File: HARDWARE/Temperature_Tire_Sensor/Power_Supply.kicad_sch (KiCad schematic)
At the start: 8 parts

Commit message: A completed schematic
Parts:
- removed C?: 0.1uF, symbol Device:C
- removed C?: 47nF, symbol Device:C
- removed C?: 10uF, symbol Device:C
- removed IC?: NCV8775CDT33RKG, NCV8775CDT33RKG, symbol NCV8775CDT33RKG:NCV8775CDT33RKG
- removed R?: 5k, symbol Device:R_US
- added C?: 10u <3.4Ohm, symbol Device:C
- added FB?: 60R@100MHz, symbol Device:FerriteBead_Small
- added U?: MIC5236, symbol Regulator_Linear:LP38512TJ-1.8
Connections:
- net +24V: now also U?.1 (EN), U?.2 (IN)
- net +3V3: now also C?.1, FB?.1, U?.4 (OUT); no longer C?.1, U?.1 (VIN), U?.3 (EN)
- net GND: now also C?.2, U?.3 (GND), U?.6 (GND)
- new net: C?.1, FB?.2, U?.1 (VIN), U?.3 (EN)
- no-connect marks 0 -> 1

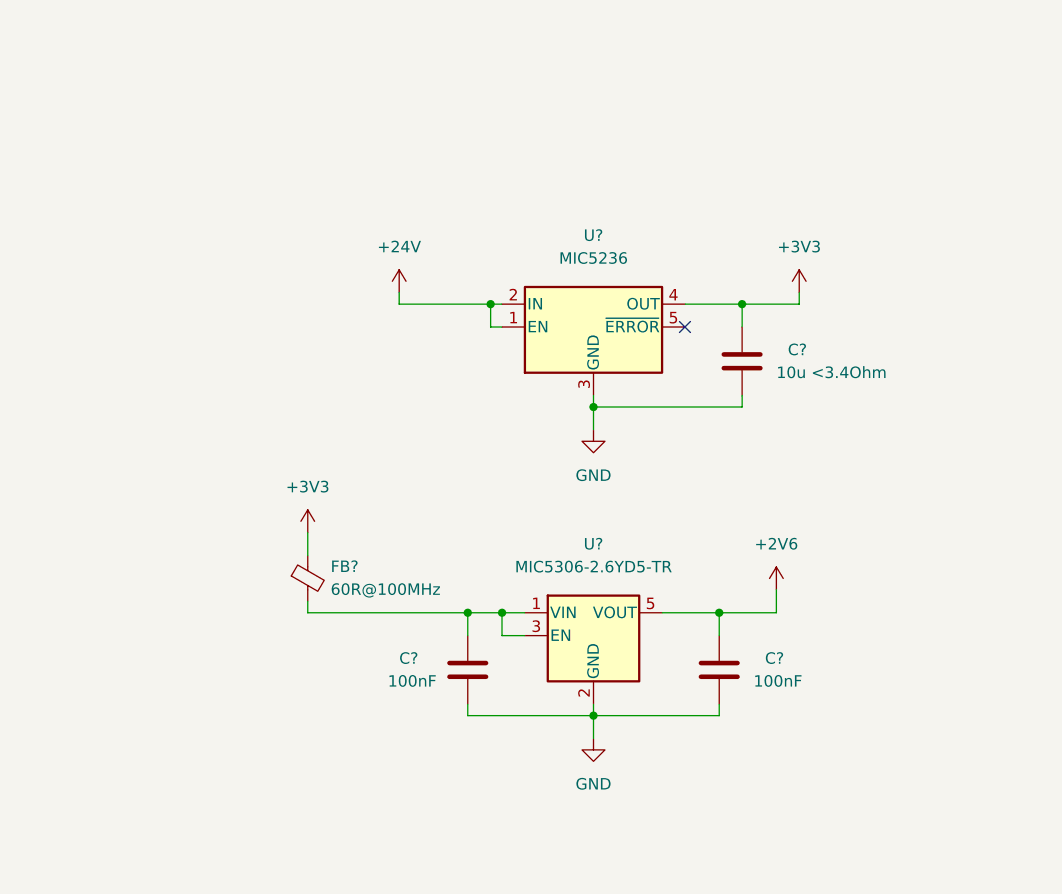
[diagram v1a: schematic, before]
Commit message: Changed the used type of labels and added power flags
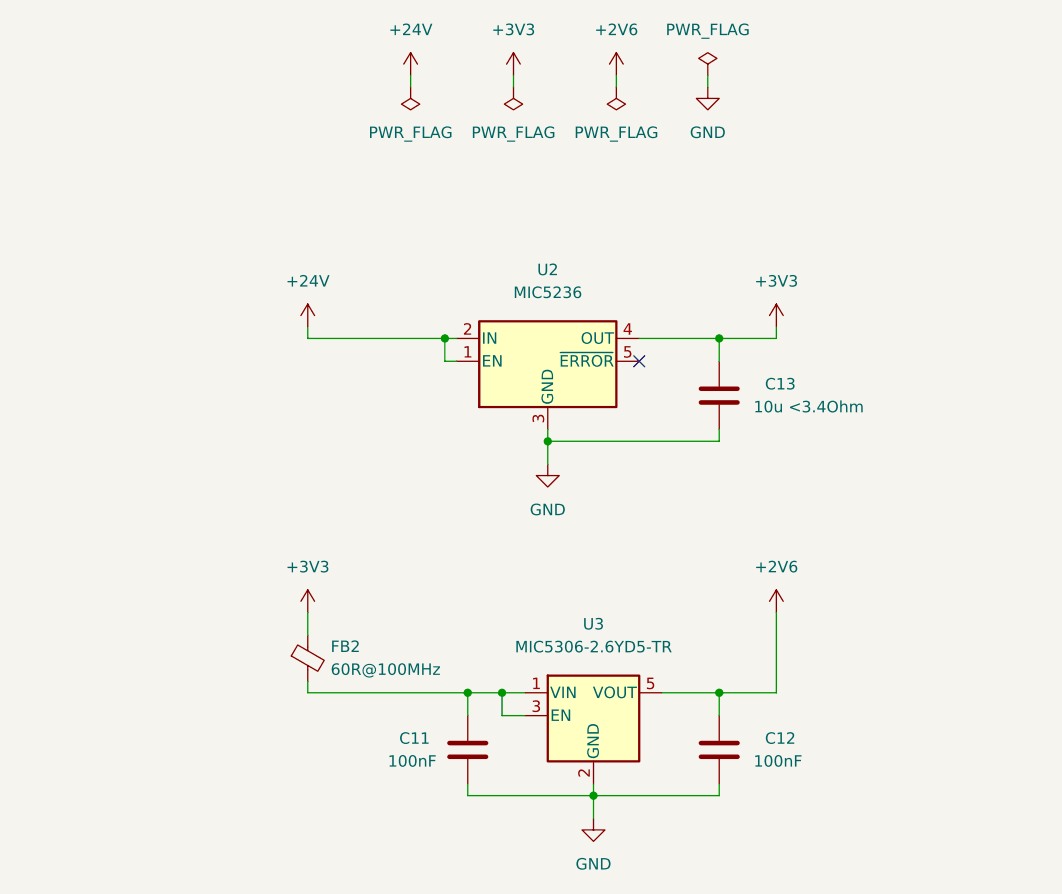
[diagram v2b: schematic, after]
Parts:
- gave numbers to parts that had none: 6
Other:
- moved on the sheet: C11, C12, C13, FB2, U2, U3

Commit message: Added all of the footprints
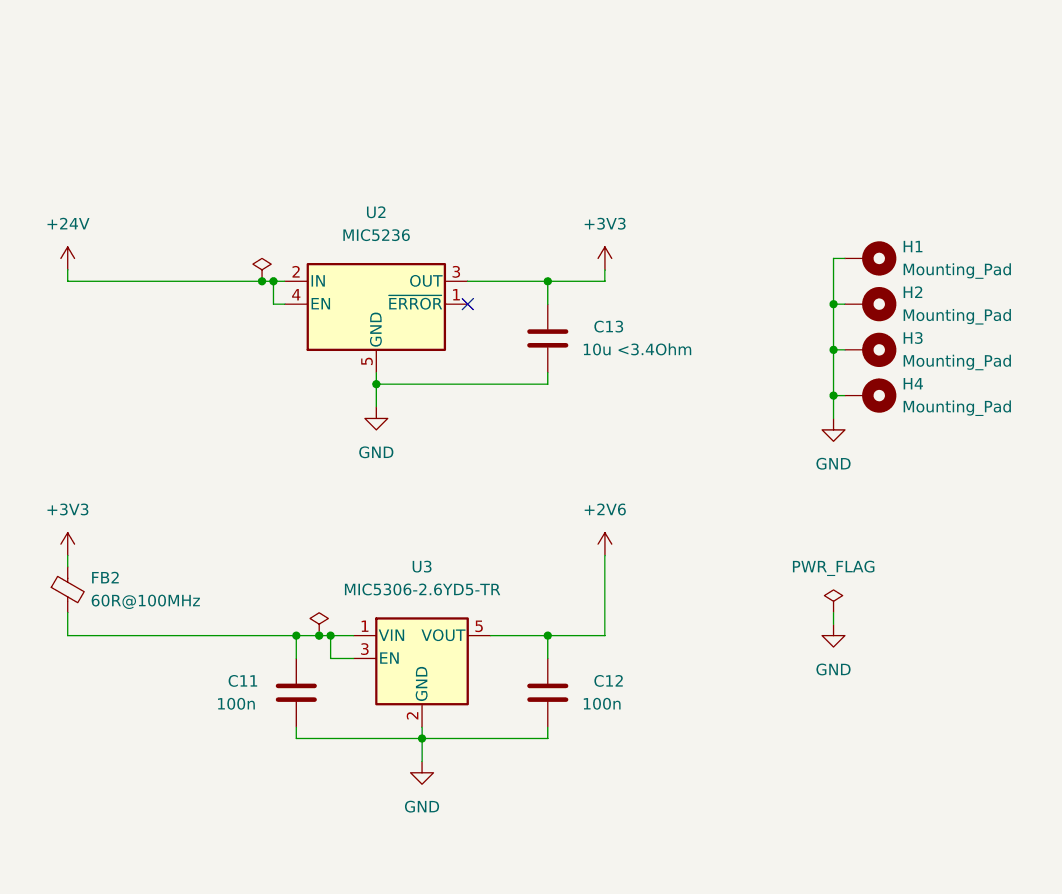
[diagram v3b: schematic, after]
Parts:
- added H1, H2, H3, H4: Mounting_Pad, MountingHole:MountingHole_3.2mm_M3_Pad_Via, symbol Mechanical:MountingHole_Pad
- C11, C12: value 100nF -> 100n; footprint (none) -> Capacitor_SMD:C_0603_1608Metric
- C13: footprint (none) -> Capacitor_SMD:C_0603_1608Metric
- FB2: footprint (none) -> Inductor_SMD:L_0603_1608Metric
- U2: footprint (none) -> Package_SO:SOIC-8_3.9x4.9mm_P1.27mm
- U3: footprint MIC5306-2.6YD5-TR -> TSOT23-5:TSOT-23-5
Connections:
- net +24V: now also U2.4 (EN); no longer U2.1 (EN)
- net +3V3: now also U2.3 (OUT); no longer U2.4 (OUT)
- net GND: now also U2.5 (GND), H1.1, H2.1, H3.1, H4.1; no longer U2.3 (GND), U2.6 (GND)
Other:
- moved on the sheet: C11, C12, C13, FB2, U2, U3

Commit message: pcb layout half done
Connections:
- net GND: now also U2.6 (GND), U2.7 (GND), U2.8 (GND)
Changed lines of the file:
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@@
       (effects (font (size 1.27 1.27)) hide)
     )
+    (pin "1")
+    (pin "2")
+    (pin "3")
     (pin "4")
-    (pin "2")
     (pin "5")
-    (pin "3")
-    (pin "1")
+    (pin "6")
+    (pin "7")
+    (pin "8")
   )
   (symbol (lib_id "Mechanical:MountingHole_Pad") (at 180.34 87.63 270) (unit 1)

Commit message: pcb layout done - waiting for the confirmation of layout V1
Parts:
- H1, H2, H3, H4: footprint MountingHole:MountingHole_3.2mm_M3_Pad_Via -> MountingHole:MountingHole_2.7mm_M2.5_ISO14580_Pad
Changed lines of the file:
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@@
       (effects (font (size 1.27 1.27)) (justify left))
     )
-    (property "Footprint" "MountingHole:MountingHole_3.2mm_M3_Pad_Via" (id 2) (at 180.34 77.47 0)
+    (property "Footprint" "MountingHole:MountingHole_2.7mm_M2.5_ISO14580_Pad" (id 2) (at 180.34 77.47 0)
       (effects (font (size 1.27 1.27)) hide)
     )
@@
       (effects (font (size 1.27 1.27)) (justify left))
     )
-    (property "Footprint" "MountingHole:MountingHole_3.2mm_M3_Pad_Via" (id 2) (at 180.34 87.63 0)
+    (property "Footprint" "MountingHole:MountingHole_2.7mm_M2.5_ISO14580_Pad" (id 2) (at 180.34 87.63 0)
       (effects (font (size 1.27 1.27)) hide)
     )
@@
       (effects (font (size 1.27 1.27)) (justify left))
     )
-    (property "Footprint" "MountingHole:MountingHole_3.2mm_M3_Pad_Via" (id 2) (at 180.34 92.71 0)
+    (property "Footprint" "MountingHole:MountingHole_2.7mm_M2.5_ISO14580_Pad" (id 2) (at 180.34 92.71 0)
       (effects (font (size 1.27 1.27)) hide)
     )
@@
       (effects (font (size 1.27 1.27)) (justify left))
     )
-    (property "Footprint" "MountingHole:MountingHole_3.2mm_M3_Pad_Via" (id 2) (at 180.34 82.55 0)
+    (property "Footprint" "MountingHole:MountingHole_2.7mm_M2.5_ISO14580_Pad" (id 2) (at 180.34 82.55 0)
       (effects (font (size 1.27 1.27)) hide)
     )

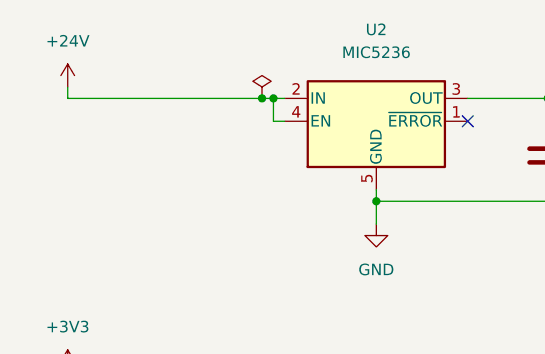
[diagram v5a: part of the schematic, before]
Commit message: Power planes has been added
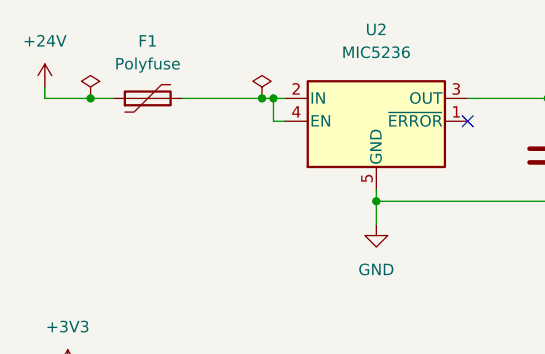
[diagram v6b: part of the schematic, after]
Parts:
- added F1: Polyfuse, Fuse:Fuse_0805_2012Metric, symbol Device:Polyfuse
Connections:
- net +24V: now also F1.1; no longer U2.2 (IN), U2.4 (EN)
- new net: F1.2, U2.2 (IN), U2.4 (EN)
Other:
- title: (none) -> Power supply
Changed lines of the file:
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@@
 (kicad_sch (version 20211123) (generator eeschema)
   (paper "A4")
+  (title_block
+    (title "Power supply")
+  )
+  (junction (at 113.03 80.01) (diameter 0) (color 0 0 0 0)
+  )
   (junction (at 130.81 130.81) (diameter 0) (color 0 0 0 0)
   )
@@
   (junction (at 116.84 119.38) (diameter 0) (color 0 0 0 0)
   )
-  (junction (at 113.03 80.01) (diameter 0) (color 0 0 0 0)
-  )
   (junction (at 176.53 82.55) (diameter 0) (color 0 0 0 0)
   )
   (junction (at 114.3 80.01) (diameter 0) (color 0 0 0 0)
+  )
+  (junction (at 93.98 80.01) (diameter 0) (color 0 0 0 0)
   )
   (junction (at 119.38 119.38) (diameter 0) (color 0 0 0 0)
@@
     (stroke (width 0) (type default) (color 0 0 0 0))
   )
+  (wire (pts (xy 88.9 78.74) (xy 88.9 80.01))
+    (stroke (width 0) (type default) (color 0 0 0 0))
+  )
   (wire (pts (xy 91.44 110.49) (xy 91.44 111.76))
     (stroke (width 0) (type default) (color 0 0 0 0))
@@
     (stroke (width 0) (type default) (color 0 0 0 0))
   )
+  (wire (pts (xy 104.14 80.01) (xy 113.03 80.01))
+    (stroke (width 0) (type default) (color 0 0 0 0))
+  )
   (wire (pts (xy 119.38 119.38) (xy 120.65 119.38))
     (stroke (width 0) (type default) (color 0 0 0 0))
@@
     (stroke (width 0) (type default) (color 0 0 0 0))
   )
+  (wire (pts (xy 93.98 80.01) (xy 96.52 80.01))
+    (stroke (width 0) (type default) (color 0 0 0 0))
+  )
   (wire (pts (xy 114.3 82.55) (xy 114.3 80.01))
     (stroke (width 0) (type default) (color 0 0 0 0))
@@
     (stroke (width 0) (type default) (color 0 0 0 0))
   )
-  (wire (pts (xy 91.44 80.01) (xy 113.03 80.01))
+  (wire (pts (xy 88.9 80.01) (xy 93.98 80.01))
     (stroke (width 0) (type default) (color 0 0 0 0))
   )
@@
   )
   (wire (pts (xy 144.78 129.54) (xy 144.78 130.81))
-    (stroke (width 0) (type default) (color 0 0 0 0))
-  )
-  (wire (pts (xy 91.44 80.01) (xy 91.44 78.74))
     (stroke (width 0) (type default) (color 0 0 0 0))
   )
@@
     )
     (pin "1")
+  )
+  (symbol (lib_id "Device:Polyfuse") (at 100.33 80.01 90) (unit 1)
+    (in_bom yes) (on_board yes) (fields_autoplaced)
+    (property "Reference" "F1" (id 0) (at 100.33 73.66 90))
+    (property "Value" "Polyfuse" (id 1) (at 100.33 76.2 90))
+    (property "Footprint" "Fuse:Fuse_0805_2012Metric" (id 2) (at 105.41 78.74 0)
+      (effects (font (size 1.27 1.27)) (justify left) hide)
+    )
+    (property "Datasheet" "~" (id 3) (at 100.33 80.01 0)
+      (effects (font (size 1.27 1.27)) hide)
+    )
+    (pin "1")
+    (pin "2")
   )
   (symbol (lib_id "power:PWR_FLAG") (at 176.53 116.84 0) (unit 1)
@@
     (pin "1")
   )
-  (symbol (lib_id "power:+24V") (at 91.44 78.74 0) (unit 1)
-    (in_bom yes) (on_board yes)
-    (property "Reference" "#PWR0105" (id 0) (at 91.44 82.55 0)
-      (effects (font (size 1.27 1.27)) hide)
-    )
-    (property "Value" "+24V" (id 1) (at 91.44 73.66 0))
-    (property "Footprint" "" (id 2) (at 91.44 78.74 0)
-      (effects (font (size 1.27 1.27)) hide)
-    )
-    (property "Datasheet" "" (id 3) (at 91.44 78.74 0)
+  (symbol (lib_id "power:+24V") (at 88.9 78.74 0) (unit 1)
+    (in_bom yes) (on_board yes)
+    (property "Reference" "#PWR0105" (id 0) (at 88.9 82.55 0)
+      (effects (font (size 1.27 1.27)) hide)
+    )
+    (property "Value" "+24V" (id 1) (at 88.9 73.66 0))
+    (property "Footprint" "" (id 2) (at 88.9 78.74 0)
+      (effects (font (size 1.27 1.27)) hide)
+    )
+    (property "Datasheet" "" (id 3) (at 88.9 78.74 0)
       (effects (font (size 1.27 1.27)) hide)
     )
@@
       (effects (font (size 1.27 1.27)) hide)
     )
+    (pin "1")
+  )
+  (symbol (lib_id "power:PWR_FLAG") (at 93.98 80.01 0) (unit 1)
+    (in_bom yes) (on_board yes) (fields_autoplaced)
+    (property "Reference" "#FLG0103" (id 0) (at 93.98 78.105 0)
+      (effects (font (size 1.27 1.27)) hide)
+    )
+    (property "Value" "PWR_FLAG" (id 1) (at 93.98 74.93 0)
+      (effects (font (size 1.27 1.27)) hide)
+    )
+    (property "Footprint" "" (id 2) (at 93.98 80.01 0)
+      (effects (font (size 1.27 1.27)) hide)
+    )
+    (property "Datasheet" "~" (id 3) (at 93.98 80.01 0)
+      (effects (font (size 1.27 1.27)) hide)
+    )
